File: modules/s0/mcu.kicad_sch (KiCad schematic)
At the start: 6 parts, among them SW1 SW_Push, U1 ESP32-C3-MINI-1U-H4

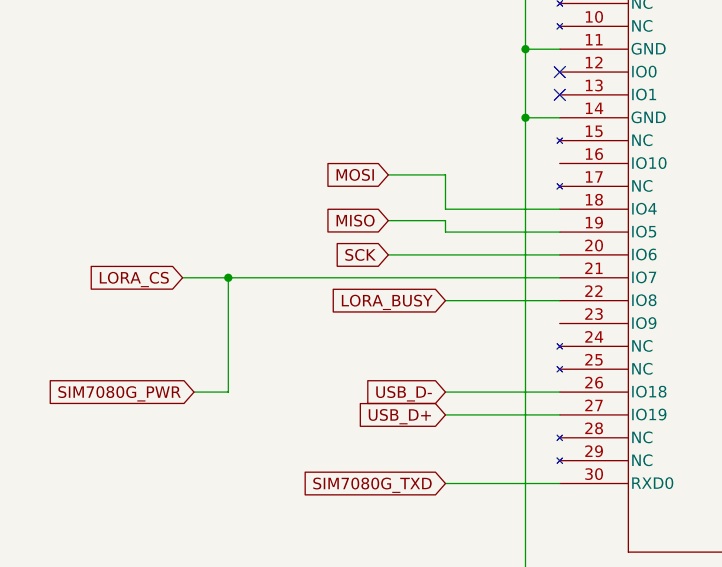
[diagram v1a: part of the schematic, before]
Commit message: chore:Modify BOM in production
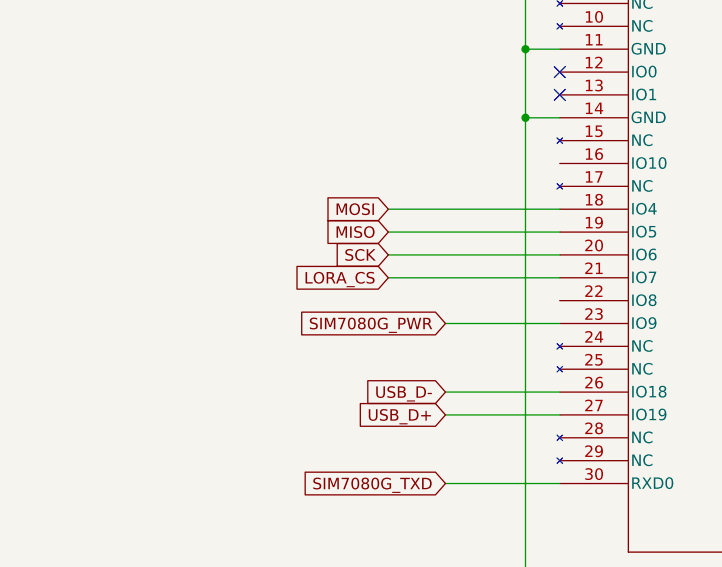
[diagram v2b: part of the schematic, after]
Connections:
- net SIM7080G_PWR: now reaches U1.23 (IO9)
- net LORA_BUSY: no longer names the net of U1.22 (IO8)
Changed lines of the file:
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@@
-	)
-	(junction
-		(at 48.26 121.92)
-		(diameter 0)
-		(color 0 0 0 0)
 	)
 	(junction
@@
 	(wire
 		(pts
-			(xy 72.39 110.49) (xy 72.39 114.3)
-		)
-		(stroke
-			(width 0)
-			(type default)
-		)
-	)
-	(wire
-		(pts
 			(xy 72.39 134.62) (xy 85.09 134.62)
 		)
@@
 	(wire
 		(pts
-			(xy 72.39 115.57) (xy 72.39 116.84)
-		)
-		(stroke
-			(width 0)
-			(type default)
-		)
-	)
-	(wire
-		(pts
-			(xy 72.39 114.3) (xy 85.09 114.3)
-		)
-		(stroke
-			(width 0)
-			(type default)
-		)
-	)
-	(wire
-		(pts
 			(xy 125.73 127) (xy 125.73 129.54)
 		)
@@
 	(wire
 		(pts
-			(xy 44.45 134.62) (xy 48.26 134.62)
-		)
-		(stroke
-			(width 0)
-			(type default)
-		)
-	)
-	(wire
-		(pts
 			(xy 81.28 104.14) (xy 85.09 104.14)
 		)
@@
 	(wire
 		(pts
-			(xy 43.18 121.92) (xy 48.26 121.92)
+			(xy 66.04 121.92) (xy 85.09 121.92)
 		)
 		(stroke
@@
 	(wire
 		(pts
-			(xy 48.26 121.92) (xy 48.26 134.62)
-		)
-		(stroke
-			(width 0)
-			(type default)
-		)
-	)
-	(wire
-		(pts
 			(xy 242.57 107.95) (xy 242.57 114.3)
 		)
@@
 	(wire
 		(pts
+			(xy 72.39 127) (xy 85.09 127)
+		)
+		(stroke
+			(width 0)
+			(type default)
+		)
+	)
+	(wire
+		(pts
 			(xy 242.57 139.7) (xy 242.57 148.59)
 		)
@@
 	(wire
 		(pts
-			(xy 66.04 110.49) (xy 72.39 110.49)
+			(xy 66.04 114.3) (xy 85.09 114.3)
 		)
 		(stroke
@@
 	(wire
 		(pts
-			(xy 72.39 116.84) (xy 85.09 116.84)
-		)
-		(stroke
-			(width 0)
-			(type default)
-		)
-	)
-	(wire
-		(pts
 			(xy 81.28 104.14) (xy 81.28 162.56)
 		)
@@
 	(wire
 		(pts
-			(xy 66.04 115.57) (xy 72.39 115.57)
+			(xy 66.04 116.84) (xy 85.09 116.84)
 		)
 		(stroke
@@
 	(wire
 		(pts
-			(xy 48.26 121.92) (xy 85.09 121.92)
-		)
-		(stroke
-			(width 0)
-			(type default)
-		)
-	)
-	(wire
-		(pts
 			(xy 218.44 41.91) (xy 218.44 45.72)
 		)
@@
 		(pts
 			(xy 73.66 76.2) (xy 73.66 68.58)
-		)
-		(stroke
-			(width 0)
-			(type default)
-		)
-	)
-	(wire
-		(pts
-			(xy 72.39 124.46) (xy 85.09 124.46)
 		)
 		(stroke
@@
 	(global_label "LORA_CS"
 		(shape input)
-		(at 43.18 121.92 180)
+		(at 66.04 121.92 180)
 		(fields_autoplaced yes)
 		(effects
@@
 		)
 		(property "Intersheetrefs" "${INTERSHEET_REFS}"
-			(at 32.0305 121.92 0)
+			(at 54.8905 121.92 0)
 			(effects
 				(font
@@
 	(global_label "MISO"
 		(shape input)
-		(at 66.04 115.57 180)
+		(at 66.04 116.84 180)
 		(fields_autoplaced yes)
 		(effects
@@
 		)
 		(property "Intersheetrefs" "${INTERSHEET_REFS}"
-			(at 58.4586 115.57 0)
+			(at 58.4586 116.84 0)
 			(effects
 				(font
@@
 		)
 	)
-	(global_label "LORA_BUSY"
-		(shape input)
-		(at 72.39 124.46 180)
+	(global_label "USB_D+"
+		(shape input)
+		(at 72.39 137.16 180)
 		(fields_autoplaced yes)
 		(effects
@@
 		)
 		(property "Intersheetrefs" "${INTERSHEET_REFS}"
-			(at 58.8214 124.46 0)
+			(at 61.7848 137.16 0)
 			(effects
 				(font
@@
 		)
 	)
-	(global_label "USB_D+"
-		(shape input)
-		(at 72.39 137.16 180)
+	(global_label "SIM7080G_PWR"
+		(shape input)
+		(at 72.39 127 180)
 		(fields_autoplaced yes)
 		(effects
@@
 		)
 		(property "Intersheetrefs" "${INTERSHEET_REFS}"
-			(at 61.7848 137.16 0)
-			(effects
-				(font
-					(size 1.27 1.27)
-				)
-				(justify right)
-				(hide yes)
-			)
-		)
-	)
-	(global_label "SIM7080G_PWR"
-		(shape input)
-		(at 44.45 134.62 180)
-		(fields_autoplaced yes)
-		(effects
-			(font
-				(size 1.27 1.27)
-			)
-			(justify right)
-		)
-		(property "Intersheetrefs" "${INTERSHEET_REFS}"
-			(at 27.1321 134.62 0)
+			(at 55.0721 127 0)
 			(effects
 				(font
@@
 	(global_label "MOSI"
 		(shape input)
-		(at 66.04 110.49 180)
+		(at 66.04 114.3 180)
 		(fields_autoplaced yes)
 		(effects
@@
 		)
 		(property "Intersheetrefs" "${INTERSHEET_REFS}"
-			(at 58.4586 110.49 0)
-			(effects
-				(font
+			(at 58.4586 114.3 0)
+			(effects
+				(font

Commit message: Modified Schematics and BOM
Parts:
- renumbered C11 to C13, C12 to C14, C13 to C15, U1 to U6
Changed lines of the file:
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@@
 		(dnp no)
 		(fields_autoplaced yes)
-		(property "Reference" "#PWR046"
+		(property "Reference" "#PWR050"
 			(at 218.44 64.77 0)
 			(effects
@@
 			(project "s0"
 				(path "/9e4c0f80-14bc-451b-8b05-b2f0d1a90e15/5c610c02-cc6e-495f-915f-5f97a877cabd"
-					(reference "#PWR046")
+					(reference "#PWR050")
 					(unit 1)
 				)
@@
 		(dnp no)
 		(fields_autoplaced yes)
-		(property "Reference" "C13"
+		(property "Reference" "C15"
 			(at 246.38 134.6199 0)
 			(effects
@@
 			(project "s0"
 				(path "/9e4c0f80-14bc-451b-8b05-b2f0d1a90e15/5c610c02-cc6e-495f-915f-5f97a877cabd"
-					(reference "C13")
+					(reference "C15")
 					(unit 1)
 				)
@@
 		(dnp no)
 		(fields_autoplaced yes)
-		(property "Reference" "#PWR050"
+		(property "Reference" "#PWR053"
 			(at 242.57 111.76 0)
 			(effects
@@
 			(project "s0"
 				(path "/9e4c0f80-14bc-451b-8b05-b2f0d1a90e15/5c610c02-cc6e-495f-915f-5f97a877cabd"
-					(reference "#PWR050")
+					(reference "#PWR053")
 					(unit 1)
 				)
@@
 		(dnp no)
 		(fields_autoplaced yes)
-		(property "Reference" "#PWR04"
+		(property "Reference" "#PWR048"
 			(at 205.74 154.94 0)
 			(effects
@@
 			(project "s0"
 				(path "/9e4c0f80-14bc-451b-8b05-b2f0d1a90e15/5c610c02-cc6e-495f-915f-5f97a877cabd"
-					(reference "#PWR04")
+					(reference "#PWR048")
 					(unit 1)
 				)
@@
 		(dnp no)
 		(fields_autoplaced yes)
-		(property "Reference" "#PWR051"
+		(property "Reference" "#PWR054"
 			(at 242.57 154.94 0)
 			(effects
@@
 			(project "s0"
 				(path "/9e4c0f80-14bc-451b-8b05-b2f0d1a90e15/5c610c02-cc6e-495f-915f-5f97a877cabd"
-					(reference "#PWR051")
+					(reference "#PWR054")
 					(unit 1)
 				)
@@
 		(dnp no)
 		(fields_autoplaced yes)
-		(property "Reference" "U1"
+		(property "Reference" "U6"
 			(at 105.41 60.96 0)
 			(effects
@@
 			(project "s0"
 				(path "/9e4c0f80-14bc-451b-8b05-b2f0d1a90e15/5c610c02-cc6e-495f-915f-5f97a877cabd"
-					(reference "U1")
+					(reference "U6")
 					(unit 1)
 				)
@@
 		(dnp no)
 		(fields_autoplaced yes)
-		(property "Reference" "#PWR045"
+		(property "Reference" "#PWR049"
 			(at 218.44 41.91 0)
 			(effects
@@
 			(project "s0"
 				(path "/9e4c0f80-14bc-451b-8b05-b2f0d1a90e15/5c610c02-cc6e-495f-915f-5f97a877cabd"
-					(reference "#PWR045")
+					(reference "#PWR049")
 					(unit 1)
 				)
@@
 		(dnp no)
 		(fields_autoplaced yes)
-		(property "Reference" "#PWR054"
+		(property "Reference" "#PWR047"
 			(at 138.43 140.97 0)
 			(effects
@@
 			(project "s0"
 				(path "/9e4c0f80-14bc-451b-8b05-b2f0d1a90e15/5c610c02-cc6e-495f-915f-5f97a877cabd"
-					(reference "#PWR054")
+					(reference "#PWR047")
 					(unit 1)
 				)
@@
 		(dnp no)
 		(fields_autoplaced yes)
-		(property "Reference" "C11"
+		(property "Reference" "C13"
 			(at 222.25 48.2599 0)
 			(effects
@@
 			(project "s0"
 				(path "/9e4c0f80-14bc-451b-8b05-b2f0d1a90e15/5c610c02-cc6e-495f-915f-5f97a877cabd"
-					(reference "C11")
+					(reference "C13")
 					(unit 1)
 				)
@@
 		(dnp no)
 		(fields_autoplaced yes)
-		(property "Reference" "C12"
+		(property "Reference" "C14"
 			(at 246.38 48.2599 0)
 			(effects
@@
 			(project "s0"
 				(path "/9e4c0f80-14bc-451b-8b05-b2f0d1a90e15/5c610c02-cc6e-495f-915f-5f97a877cabd"
-					(reference "C12")
+					(reference "C14")
 					(unit 1)
 				)
@@
 		(dnp no)
 		(fields_autoplaced yes)
-		(property "Reference" "#PWR053"
+		(property "Reference" "#PWR045"
 			(at 73.66 72.39 0)
 			(effects
@@
 			(project "s0"
 				(path "/9e4c0f80-14bc-451b-8b05-b2f0d1a90e15/5c610c02-cc6e-495f-915f-5f97a877cabd"
-					(reference "#PWR053")
+					(reference "#PWR045")
 					(unit 1)
 				)
@@
 		(dnp no)
 		(fields_autoplaced yes)
-		(property "Reference" "#PWR052"
+		(property "Reference" "#PWR046"
 			(at 81.28 168.91 0)
 			(effects
@@
 			(project "s0"
 				(path "/9e4c0f80-14bc-451b-8b05-b2f0d1a90e15/5c610c02-cc6e-495f-915f-5f97a877cabd"
-					(reference "#PWR052")
+					(reference "#PWR046")
 					(unit 1)
 				)
@@
 		(dnp no)
 		(fields_autoplaced yes)
-		(property "Reference" "#PWR049"
+		(property "Reference" "#PWR051"
 			(at 242.57 41.91 0)
 			(effects
@@
 			(project "s0"
 				(path "/9e4c0f80-14bc-451b-8b05-b2f0d1a90e15/5c610c02-cc6e-495f-915f-5f97a877cabd"
-					(reference "#PWR049")
+					(reference "#PWR051")
 					(unit 1)
 				)
@@
 		(dnp no)
 		(fields_autoplaced yes)
-		(property "Reference" "#PWR047"
+		(property "Reference" "#PWR052"
 			(at 242.57 64.77 0)
 			(effects
@@
 			(project "s0"
 				(path "/9e4c0f80-14bc-451b-8b05-b2f0d1a90e15/5c610c02-cc6e-495f-915f-5f97a877cabd"
-					(reference "#PWR047")
-					(unit 1)
-				)
+					(reference "#PWR052")
+					(unit 1)
+				)

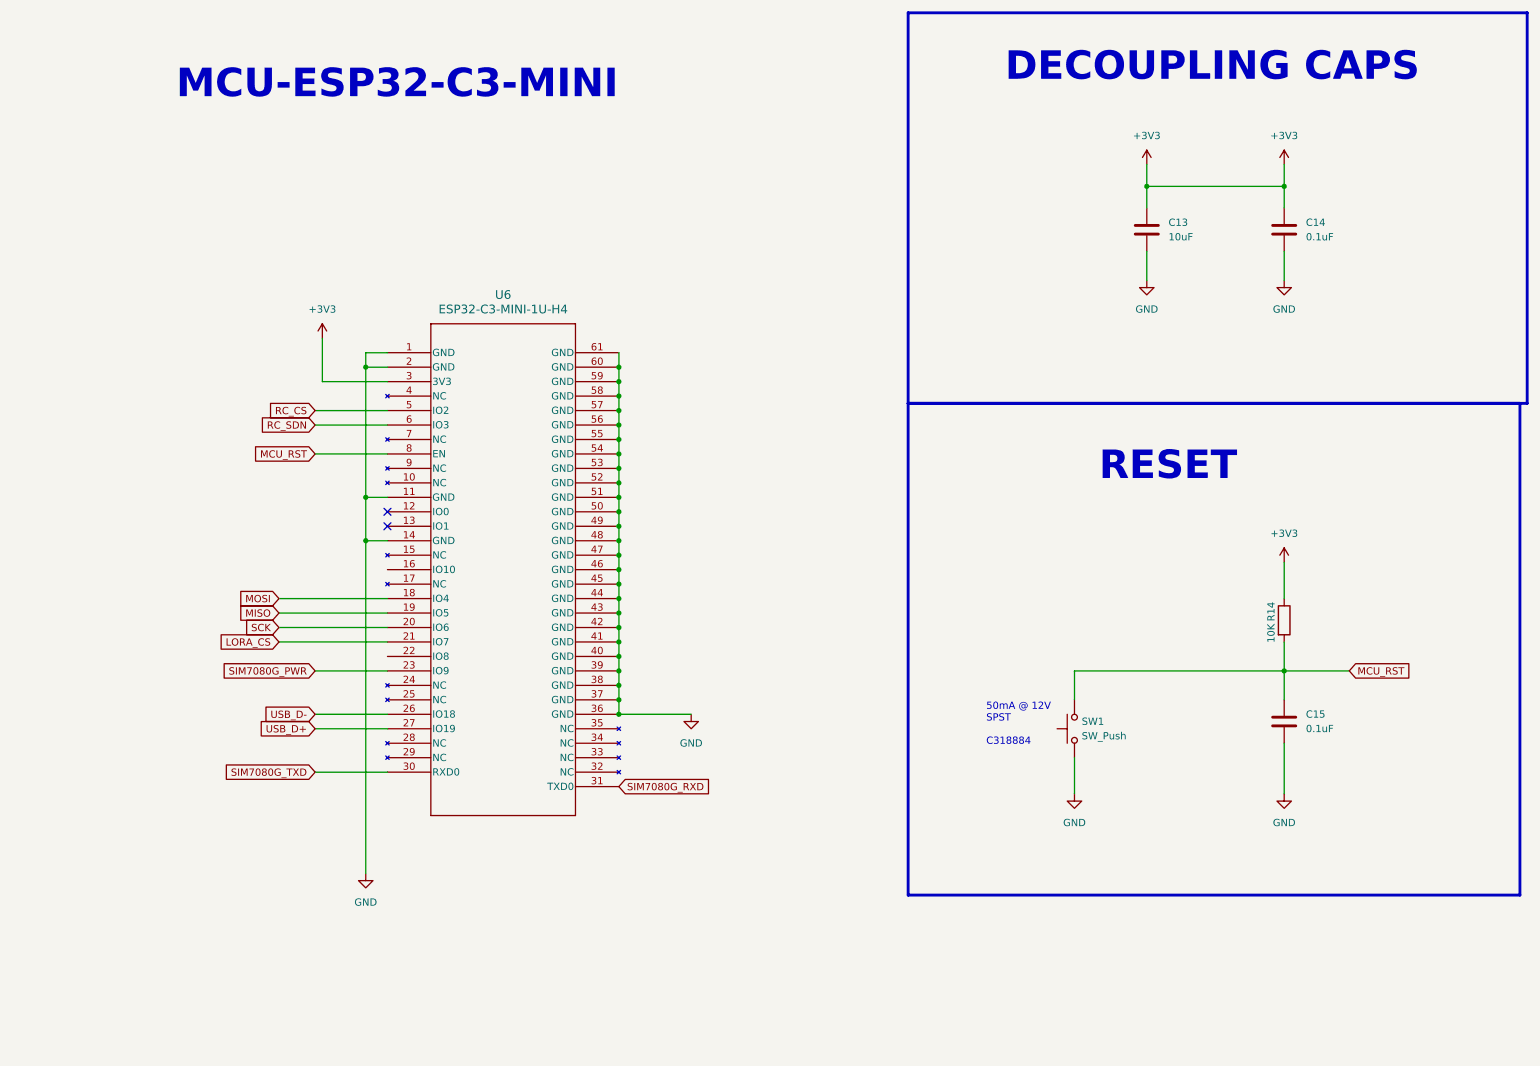
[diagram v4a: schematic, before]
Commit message: fix: add fuse, ferrite bead and fixes from gpt
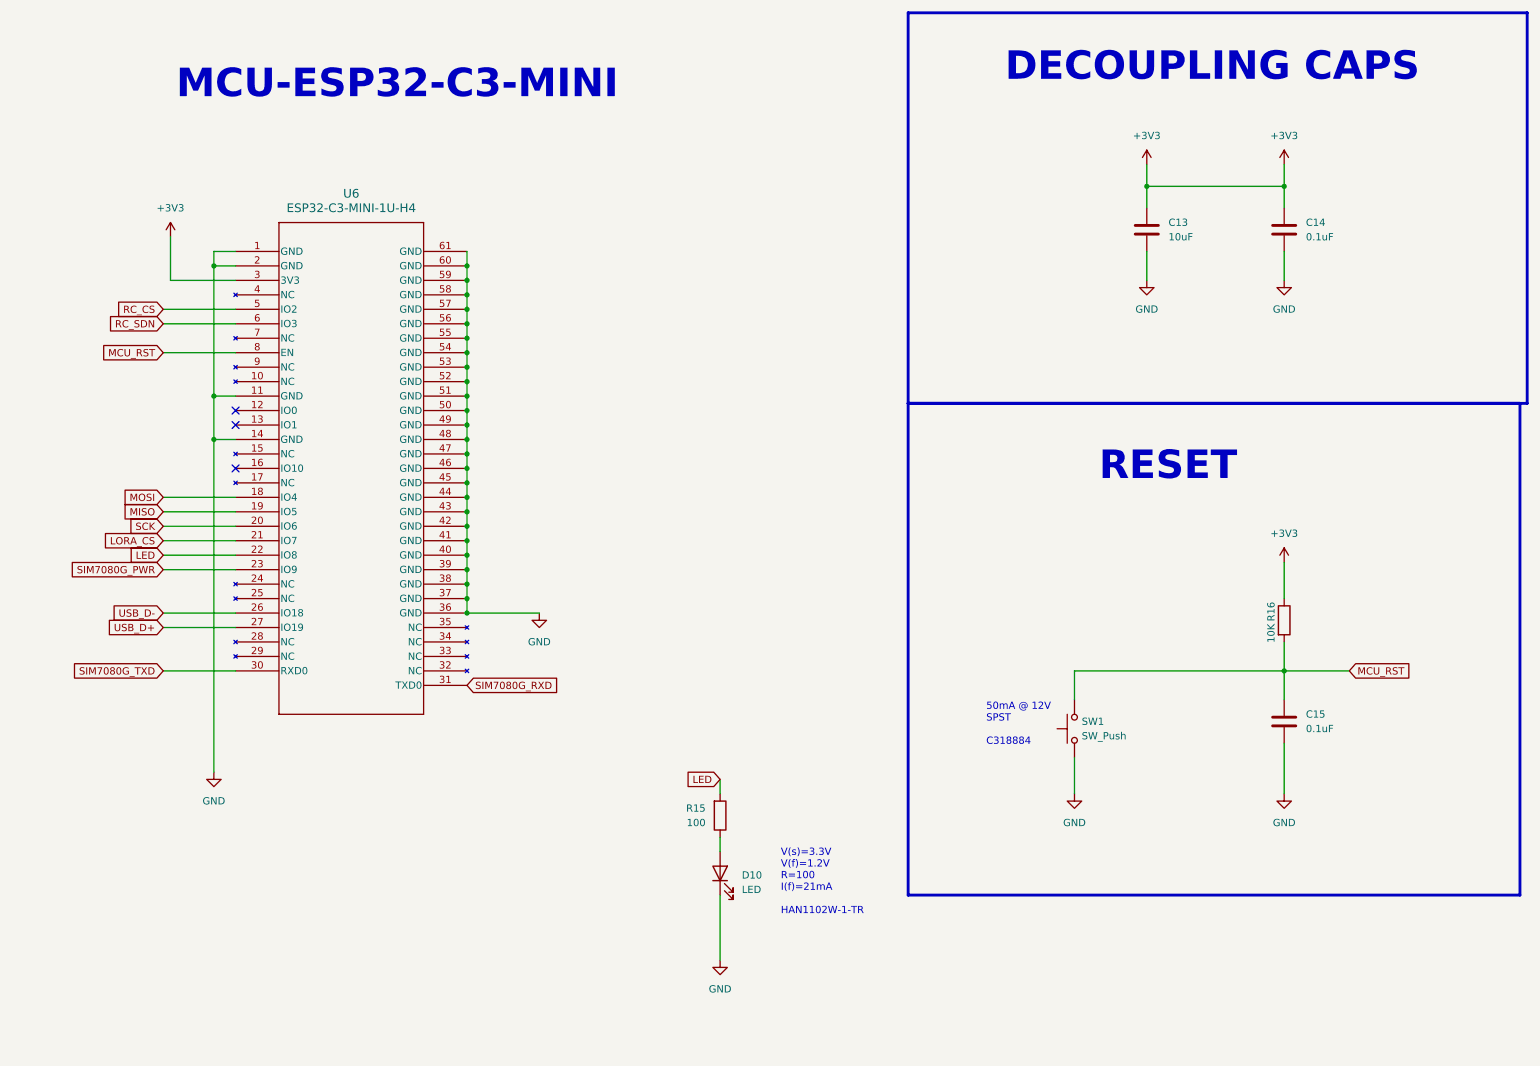
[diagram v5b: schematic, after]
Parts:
- added D10: LED, LED_SMD:LED_0603_1608Metric, symbol Device:LED
- added R15: 100, Resistor_SMD:R_0402_1005Metric, symbol Device:R
- renumbered R14 to R16
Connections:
- net GND: now also D10.1 (K)
- net LED: now reaches U6.22 (IO8)
- net LED: now also R15.2
- new net: D10.2 (A), R15.1
- no-connect marks 2 -> 3
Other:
- note added: "V(s)=3.3V V(f)=1.2V R=100 I(f)=21mA HAN1102W-1-TR"
- moved on the sheet: U6
